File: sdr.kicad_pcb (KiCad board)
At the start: 2 copper layers, 79.8 x 23.9 mm, 49 parts, among them J1 Conn_01x03_Male, J2 Conn_Coaxial, J3 Conn_01x02_Male, J4 USB_B_Mini, SW1 RST, SW2 DFU, T1 6.8u, U1 LT6231, U2 SN74CBT3253, U3 NCP1117-3.3_SOT223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

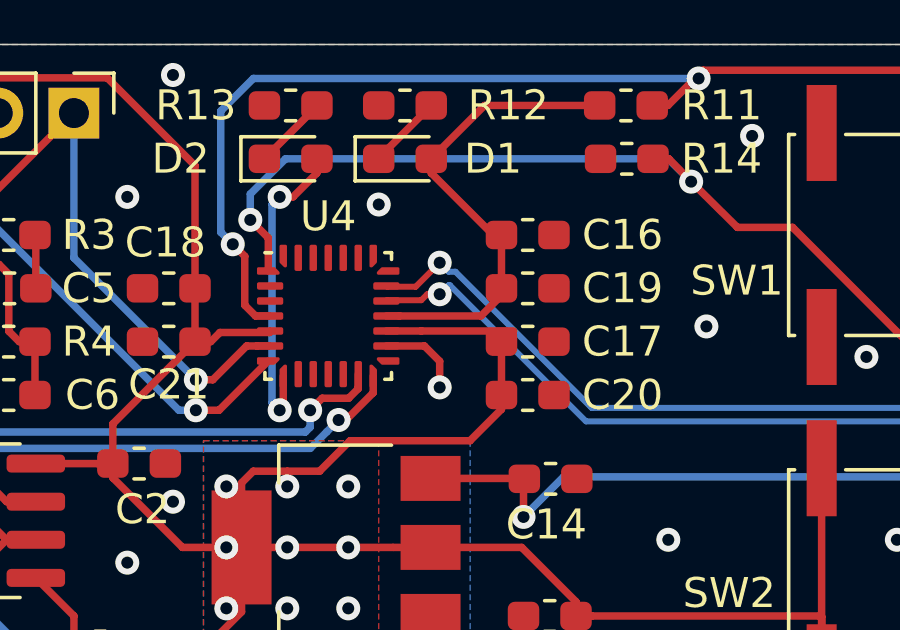
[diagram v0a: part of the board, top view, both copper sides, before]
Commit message: connect missing wire
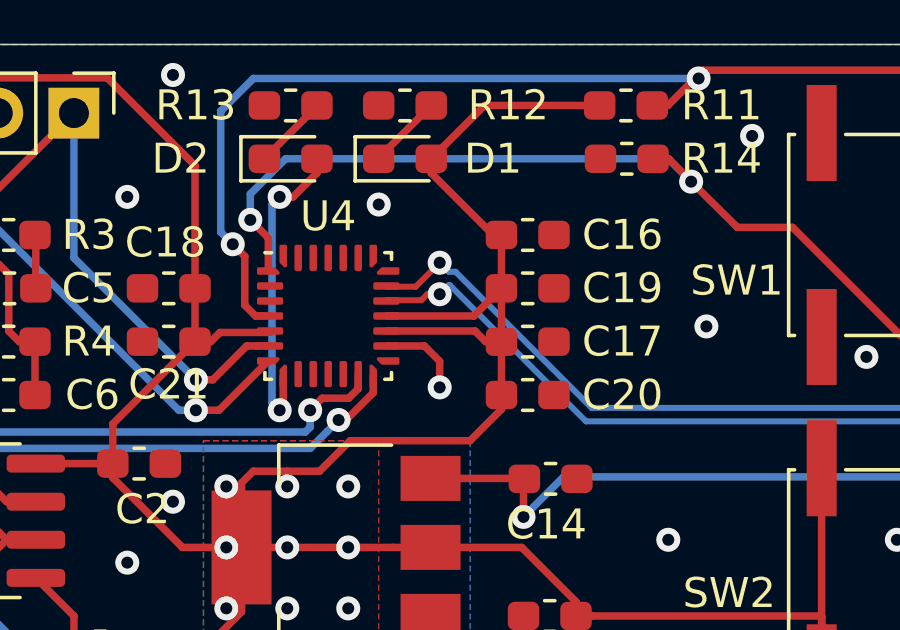
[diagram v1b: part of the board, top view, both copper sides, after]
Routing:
- net +3V3: track 116.5 -> 118.1 mm
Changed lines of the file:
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@@
     (thickness 1.6)
     (drawings 8)
-    (tracks 357)
+    (tracks 359)
     (zones 0)
     (modules 49)
@@
   (segment (start 57.404 26.806) (end 57.794 26.416) (width 0.25) (layer F.Cu) (net 2))
   (segment (start 60.004688 26.416) (end 61.020688 25.4) (width 0.25) (layer F.Cu) (net 2))
-  (segment (start 62.6675 21.2415) (end 62.23 21.2415) (width 0.25) (layer F.Cu) (net 2))
-  (segment (start 65.3835 21.2415) (end 62.6675 21.2415) (width 0.25) (layer F.Cu) (net 2))
-  (segment (start 66.305 20.32) (end 65.3835 21.2415) (width 0.25) (layer F.Cu) (net 2))
   (segment (start 63.726 16.477) (end 63.726 16.002) (width 0.25) (layer F.Cu) (net 2))
   (segment (start 65.791 18.542) (end 63.726 16.477) (width 0.25) (layer F.Cu) (net 2))
@@
   (segment (start 41.820001 13.302999) (end 37.564 17.559) (width 0.25) (layer F.Cu) (net 2))
   (segment (start 55.852 20.32) (end 55.852 16.228998) (width 0.25) (layer F.Cu) (net 2))
-  (segment (start 63.3975 21.7415) (end 62.23 21.7415) (width 0.25) (layer F.Cu) (net 2))
-  (segment (start 66.4735 21.7415) (end 63.3975 21.7415) (width 0.25) (layer F.Cu) (net 2))
   (segment (start 66.068 22.098) (end 66.068 23.876) (width 0.25) (layer F.Cu) (net 2))
   (segment (start 66.068 24.351) (end 66.068 23.876) (width 0.25) (layer F.Cu) (net 2))
@@
   (segment (start 56.896 28.956) (end 55.433 28.956) (width 0.25) (layer F.Cu) (net 2))
   (via (at 56.896 28.956) (size 0.8) (drill 0.4) (layers F.Cu B.Cu) (net 2))
+  (segment (start 66.068 20.32) (end 66.068 22.098) (width 0.25) (layer F.Cu) (net 2))
+  (segment (start 65.1865 21.7415) (end 65.543 22.098) (width 0.25) (layer F.Cu) (net 2))
+  (segment (start 65.543 22.098) (end 66.068 22.098) (width 0.25) (layer F.Cu) (net 2))
+  (segment (start 62.23 21.7415) (end 65.1865 21.7415) (width 0.25) (layer F.Cu) (net 2))
+  (segment (start 66.305 20.32) (end 66.068 20.32) (width 0.25) (layer F.Cu) (net 2))
+  (segment (start 65.1465 21.2415) (end 62.23 21.2415) (width 0.25) (layer F.Cu) (net 2))
+  (segment (start 66.068 20.32) (end 65.1465 21.2415) (width 0.25) (layer F.Cu) (net 2))
   (segment (start 23.368 14.986) (end 25.908 14.986) (width 0.25) (layer F.Cu) (net 3))
   (segment (start 25.908 14.986) (end 29.746 14.986) (width 0.25) (layer F.Cu) (net 3))
